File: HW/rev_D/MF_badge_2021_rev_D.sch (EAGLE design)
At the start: 80 parts, among them IC1 MCP73831, J1 HRO_31_M_12_USB_C, Q1 SI1308EDL-T1-GE3, Q2 DMG3415U-7, Q3 DMG3415U-7, Q4 DMG3415U-7, U1 ESP32-S2-WROOM, U2 AP2112K-3.3, X1 CAPTOUCH_10MM, X2 CAPTOUCH_10MM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

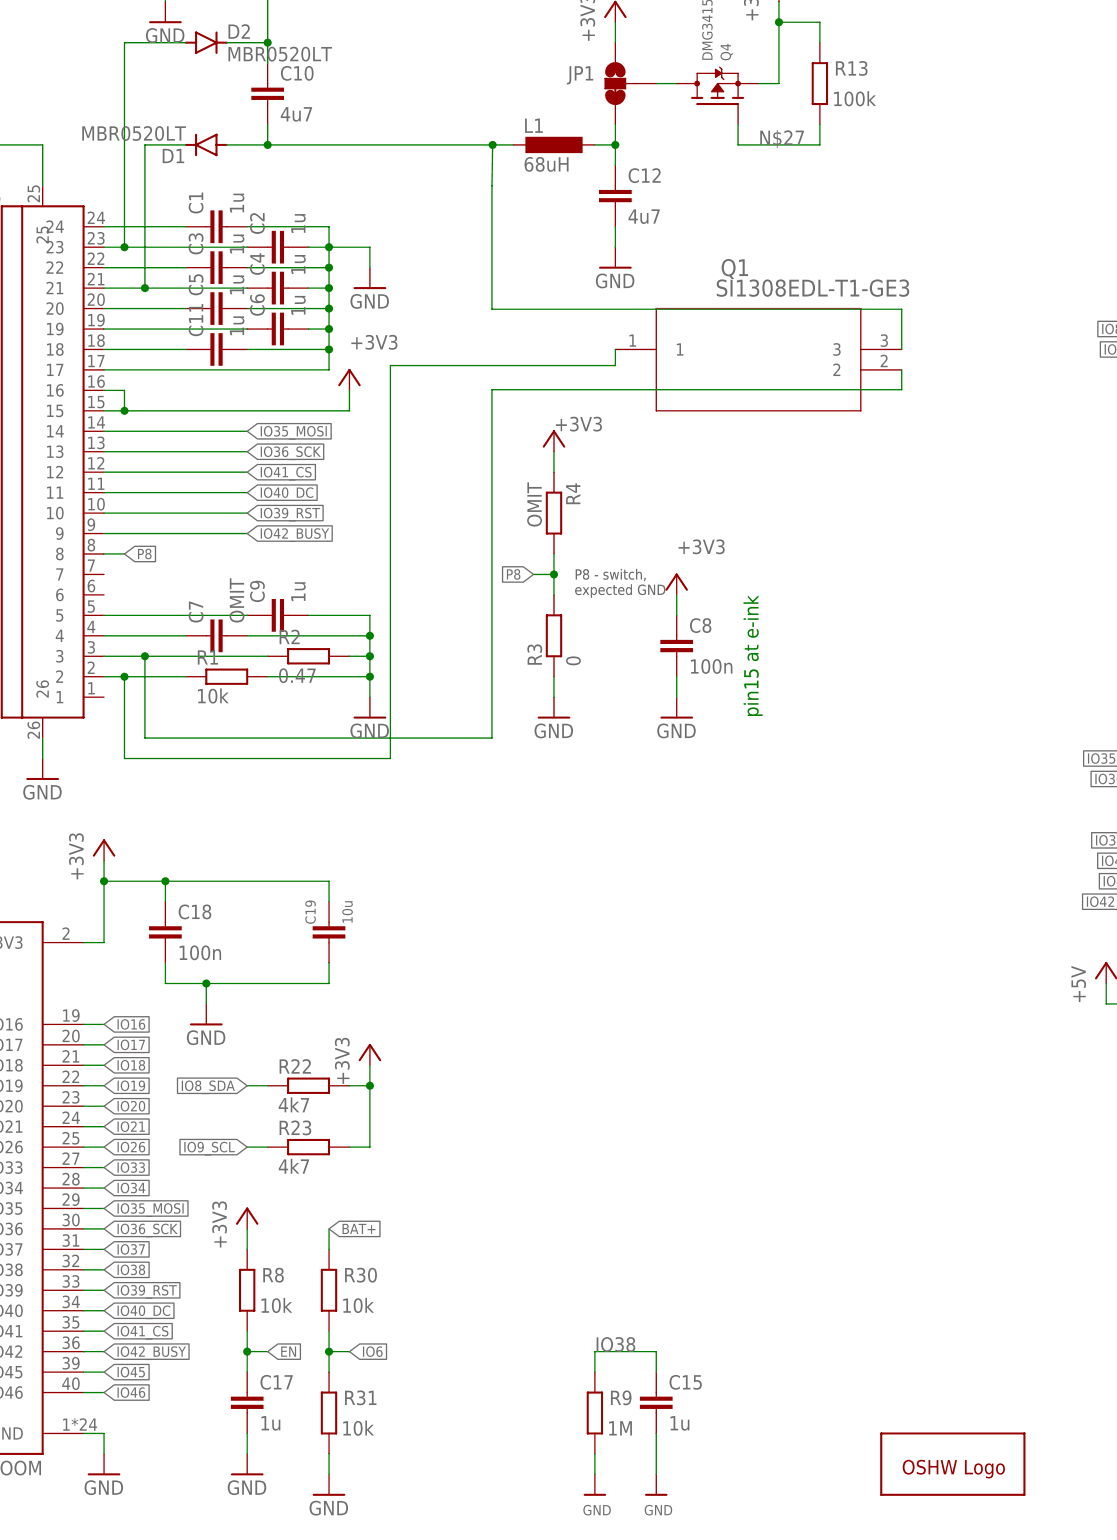
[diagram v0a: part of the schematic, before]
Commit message: Update
- removed CR2032 battery holder
- changed battery measuring circuit to save power
- add N-MOSFET to control 3V3 to e-ink displey
- changed QR to match new project address
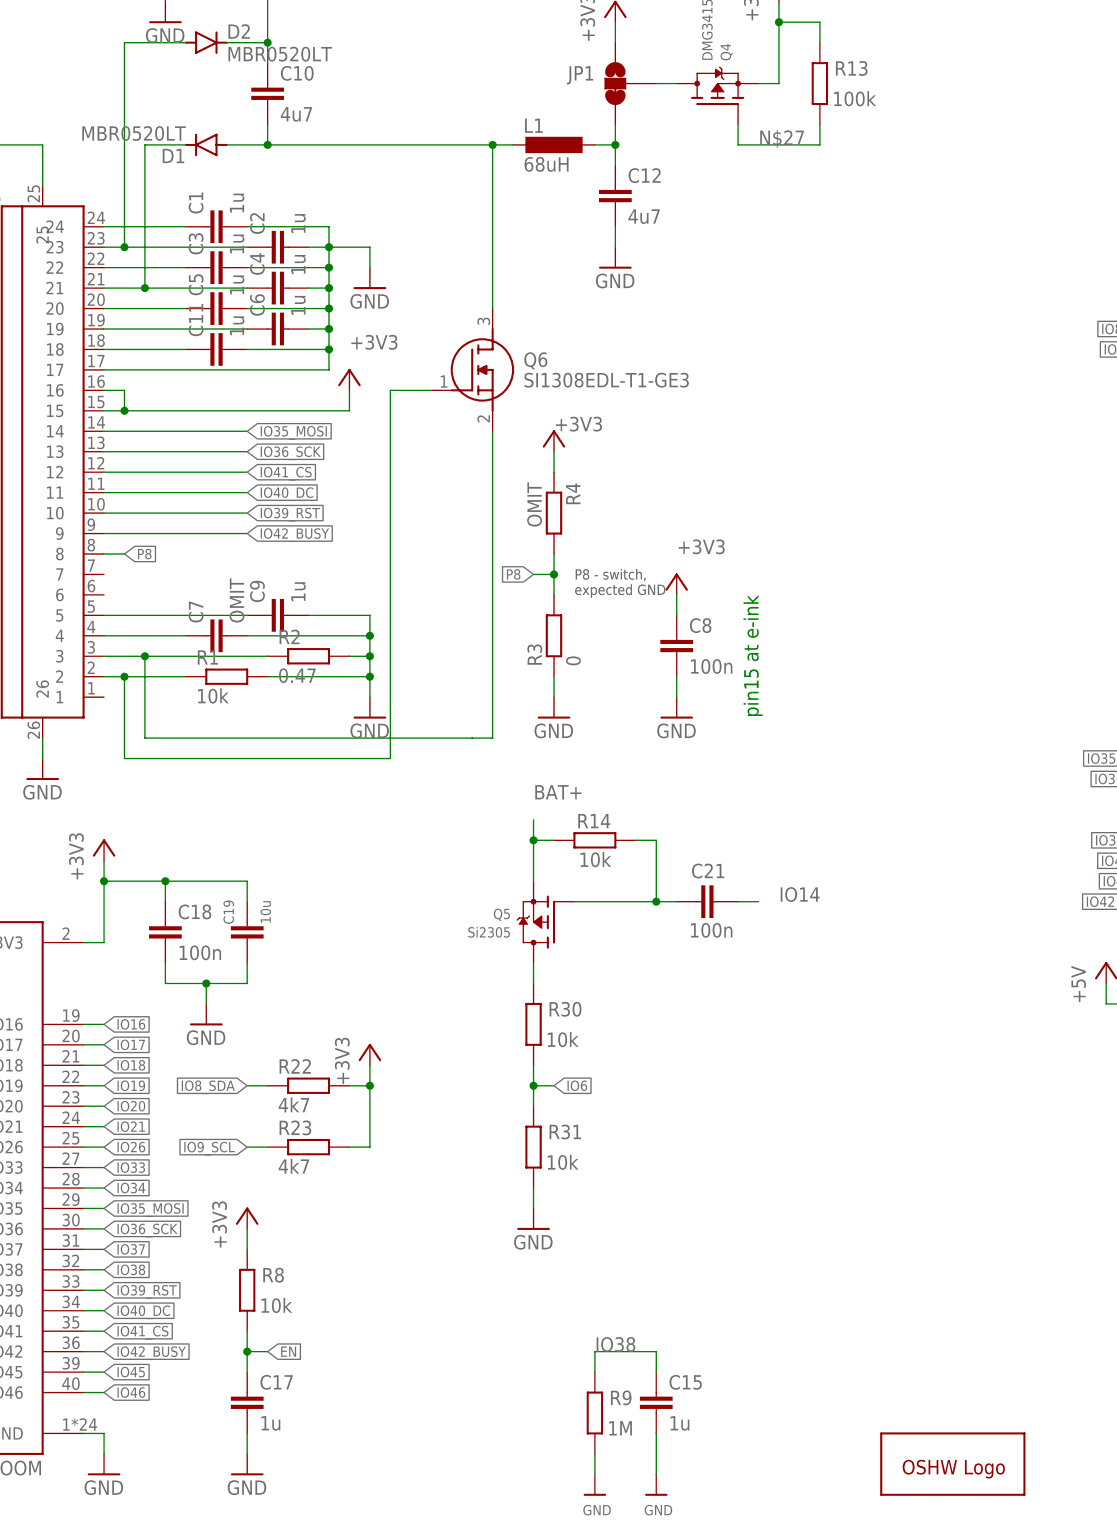
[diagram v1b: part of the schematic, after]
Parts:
- removed Q1: SI1308EDL-T1-GE3, SI1308EDL-T1-GE3:SI1308EDL-T1-GE3
- added C21: 100n, rcl:C-EUC0805
- added Q5: Si2305, microbuilder:MOSFET-P
- added Q6: SI1308EDL-T1-GE3, SamacSys_Parts:SI1308EDL-T1-GE3
- added R14: 10k, rcl:R-EU_R0805
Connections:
- new net N$79: Q5.D, R30.2
- new net N$80: C21.1, Q5.G, R14.1
- net BAT+: now also Q5.S, R14.2; no longer R30.2
- net IO14: now also C21.2
- net N$10: now also Q6.S; no longer Q1.2
- net N$13: now also Q6.G; no longer Q1.1
- net N$19: now also Q6.D; no longer Q1.3
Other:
- moved on the sheet: C19, R30, R31

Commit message: Update
- schematic cleanup
- power supply layout optimization
- changed some R and C values
- add hole for battery holder
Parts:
- C10, C12: value 4u7 -> 4u7F
- C13, C14, C16, C19, C20: value 10u -> 10uF
- C15, C17, C22, C9: value 1u -> 1uF
- C18: value 100n -> 10uF
- C21, C8: value 100n -> 100nF
- R1, R10, R11, R12, R14, R30, R31, R7, R8: value 10k -> 10K
- R13, R5: value 100k -> 10K
- R15, R16: value 5k1 -> 5K1
- R17, R18: value 22 -> 22R
- R2: value 0.47 -> 0.47R
- R22, R23: value 4k7 -> 4K7
- R6: value 1k -> 1K
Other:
- moved on the sheet: BOOT, C1, C10, C11, C12, C13, C14, C15, C16, C18, C19, C2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

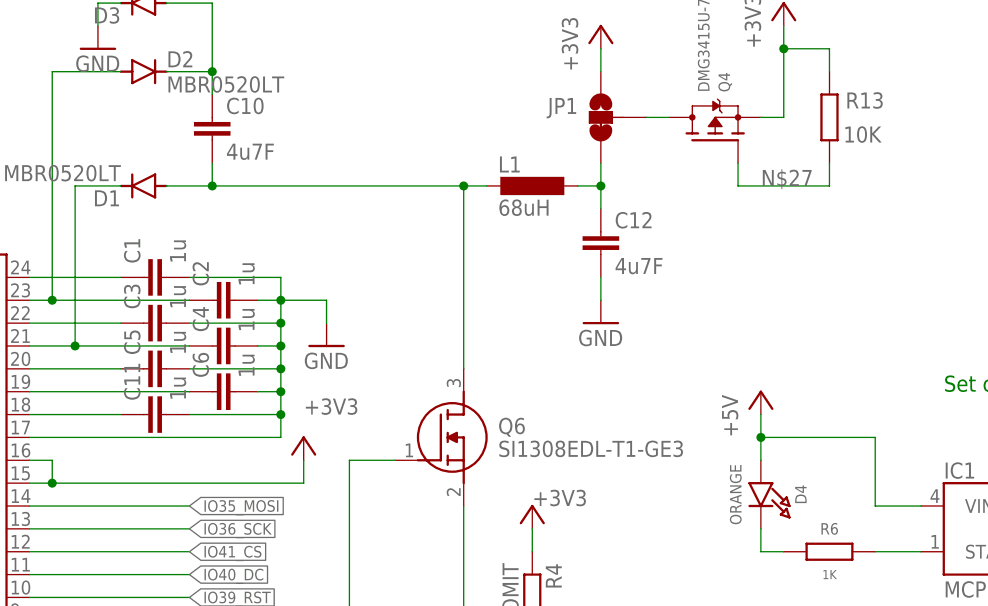
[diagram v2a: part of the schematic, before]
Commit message: Update MF_badge_2021_rev_D.sch
- forget to add it in previous commit
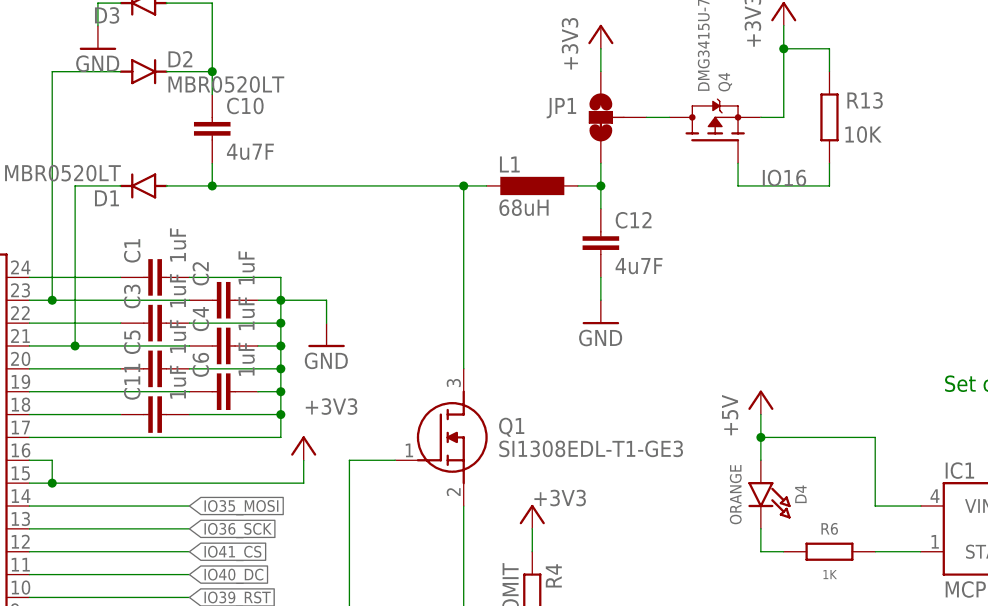
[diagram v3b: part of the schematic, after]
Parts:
- C1, C11, C2, C3, C4, C5, C6: value 1u -> 1uF
- renumbered Q6 to Q1
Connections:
- removed net N$27: Q4.G, R13.1
- net IO16: now also Q4.G, R13.1
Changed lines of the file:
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@@
 <part name="R1" library="rcl" library_urn="urn:adsk.eagle:library:334" deviceset="R-EU_" device="R0805" package3d_urn="urn:adsk.eagle:package:23553/2" value="10K"/>
 <part name="R2" library="rcl" library_urn="urn:adsk.eagle:library:334" deviceset="R-EU_" device="R0805" package3d_urn="urn:adsk.eagle:package:23553/2" value="0.47R"/>
-<part name="C1" library="rcl" library_urn="urn:adsk.eagle:library:334" deviceset="C-EU" device="C0805" package3d_urn="urn:adsk.eagle:package:23617/2" value="1u"/>
-<part name="C2" library="rcl" library_urn="urn:adsk.eagle:library:334" deviceset="C-EU" device="C0805" package3d_urn="urn:adsk.eagle:package:23617/2" value="1u"/>
-<part name="C3" library="rcl" library_urn="urn:adsk.eagle:library:334" deviceset="C-EU" device="C0805" package3d_urn="urn:adsk.eagle:package:23617/2" value="1u"/>
-<part name="C4" library="rcl" library_urn="urn:adsk.eagle:library:334" deviceset="C-EU" device="C0805" package3d_urn="urn:adsk.eagle:package:23617/2" value="1u"/>
-<part name="C5" library="rcl" library_urn="urn:adsk.eagle:library:334" deviceset="C-EU" device="C0805" package3d_urn="urn:adsk.eagle:package:23617/2" value="1u"/>
-<part name="C6" library="rcl" library_urn="urn:adsk.eagle:library:334" deviceset="C-EU" device="C0805" package3d_urn="urn:adsk.eagle:package:23617/2" value="1u"/>
+<part name="C1" library="rcl" library_urn="urn:adsk.eagle:library:334" deviceset="C-EU" device="C0805" package3d_urn="urn:adsk.eagle:package:23617/2" value="1uF"/>
+<part name="C2" library="rcl" library_urn="urn:adsk.eagle:library:334" deviceset="C-EU" device="C0805" package3d_urn="urn:adsk.eagle:package:23617/2" value="1uF"/>
+<part name="C3" library="rcl" library_urn="urn:adsk.eagle:library:334" deviceset="C-EU" device="C0805" package3d_urn="urn:adsk.eagle:package:23617/2" value="1uF"/>
+<part name="C4" library="rcl" library_urn="urn:adsk.eagle:library:334" deviceset="C-EU" device="C0805" package3d_urn="urn:adsk.eagle:package:23617/2" value="1uF"/>
+<part name="C5" library="rcl" library_urn="urn:adsk.eagle:library:334" deviceset="C-EU" device="C0805" package3d_urn="urn:adsk.eagle:package:23617/2" value="1uF"/>
+<part name="C6" library="rcl" library_urn="urn:adsk.eagle:library:334" deviceset="C-EU" device="C0805" package3d_urn="urn:adsk.eagle:package:23617/2" value="1uF"/>
 <part name="C7" library="rcl" library_urn="urn:adsk.eagle:library:334" deviceset="C-EU" device="C0805" package3d_urn="urn:adsk.eagle:package:23617/2" value="OMIT"/>
 <part name="C8" library="rcl" library_urn="urn:adsk.eagle:library:334" deviceset="C-EU" device="C0805" package3d_urn="urn:adsk.eagle:package:23617/2" value="100nF"/>
 <part name="C9" library="rcl" library_urn="urn:adsk.eagle:library:334" deviceset="C-EU" device="C0805" package3d_urn="urn:adsk.eagle:package:23617/2" value="1uF"/>
 <part name="C10" library="rcl" library_urn="urn:adsk.eagle:library:334" deviceset="C-EU" device="C0805" package3d_urn="urn:adsk.eagle:package:23617/2" value="4u7F"/>
-<part name="C11" library="rcl" library_urn="urn:adsk.eagle:library:334" deviceset="C-EU" device="C0805" package3d_urn="urn:adsk.eagle:package:23617/2" value="1u"/>
+<part name="C11" library="rcl" library_urn="urn:adsk.eagle:library:334" deviceset="C-EU" device="C0805" package3d_urn="urn:adsk.eagle:package:23617/2" value="1uF"/>
 <part name="C12" library="rcl" library_urn="urn:adsk.eagle:library:334" deviceset="C-EU" device="C0805" package3d_urn="urn:adsk.eagle:package:23617/2" value="4u7F"/>
 <part name="L1" library="rcl" library_urn="urn:adsk.eagle:library:334" deviceset="L-EU" device="L4532P" package3d_urn="urn:adsk.eagle:package:23484/1" value="68uH"/>
@@
 <part name="R14" library="rcl" library_urn="urn:adsk.eagle:library:334" deviceset="R-EU_" device="R0805" package3d_urn="urn:adsk.eagle:package:23553/2" value="10K"/>
 <part name="C21" library="rcl" library_urn="urn:adsk.eagle:library:334" deviceset="C-EU" device="C0805" package3d_urn="urn:adsk.eagle:package:23617/2" value="100nF"/>
-<part name="Q6" library="SamacSys_Parts" deviceset="SI1308EDL-T1-GE3" device=""/>
+<part name="Q1" library="SamacSys_Parts" deviceset="SI1308EDL-T1-GE3" device=""/>
 <part name="+3V13" library="supply1" library_urn="urn:adsk.eagle:library:371" deviceset="+3V3" device=""/>
 </parts>
@@
 <attribute name="VALUE" x="115.824" y="43.815" size="1.778" layer="96"/>
 </instance>
-<instance part="Q6" gate="G$1" x="63.5" y="149.86" smashed="yes">
+<instance part="Q1" gate="G$1" x="63.5" y="149.86" smashed="yes">
 <attribute name="NAME" x="74.93" y="153.67" size="1.778" layer="95" align="center-left"/>
 <attribute name="VALUE" x="74.93" y="151.13" size="1.778" layer="96" align="center-left"/>
@@
 <wire x1="27.94" y1="106.68" x2="27.94" y2="116.84" width="0.1524" layer="91"/>
 <junction x="27.94" y="116.84"/>
-<pinref part="Q6" gate="G$1" pin="S"/>
+<pinref part="Q1" gate="G$1" pin="S"/>
 <wire x1="71.12" y1="144.78" x2="71.12" y2="106.68" width="0.1524" layer="91"/>
 </segment>
@@
 <wire x1="25.4" y1="104.14" x2="25.4" y2="114.3" width="0.1524" layer="91"/>
 <junction x="25.4" y="114.3"/>
-<pinref part="Q6" gate="G$1" pin="G"/>
+<pinref part="Q1" gate="G$1" pin="G"/>
 <wire x1="63.5" y1="149.86" x2="58.42" y2="149.86" width="0.1524" layer="91"/>
 </segment>
@@
 <pinref part="GPIO2" gate="A" pin="19"/>
 </segment>
+<segment>
+<pinref part="Q4" gate="G$1" pin="G"/>
+<wire x1="101.6" y1="182.88" x2="101.6" y2="180.34" width="0.1524" layer="91"/>
+<wire x1="101.6" y1="180.34" x2="111.76" y2="180.34" width="0.1524" layer="91"/>
+<pinref part="R13" gate="G$1" pin="1"/>
+<wire x1="111.76" y1="182.88" x2="111.76" y2="180.34" width="0.1524" layer="91"/>
+<label x="104.14" y="180.34" size="1.778" layer="95"/>
+</segment>
 </net>
 <net name="IO17" class="0">
@@
 <junction x="43.18" y="180.34"/>
 <wire x1="71.12" y1="180.34" x2="73.66" y2="180.34" width="0.1524" layer="91"/>
-<pinref part="Q6" gate="G$1" pin="D"/>
+<pinref part="Q1" gate="G$1" pin="D"/>
 <wire x1="71.12" y1="160.02" x2="71.12" y2="180.34" width="0.1524" layer="91"/>
 <junction x="71.12" y="180.34"/>
@@
 </segment>
 </net>
-<net name="N$27" class="0">
-<segment>
-<pinref part="Q4" gate="G$1" pin="G"/>
-<wire x1="101.6" y1="182.88" x2="101.6" y2="180.34" width="0.1524" layer="91"/>
-<wire x1="101.6" y1="180.34" x2="111.76" y2="180.34" width="0.1524" layer="91"/>
-<pinref part="R13" gate="G$1" pin="1"/>
-<wire x1="111.76" y1="182.88" x2="111.76" y2="180.34" width="0.1524" layer="91"/>
-<label x="104.14" y="180.34" size="1.778" layer="95"/>
-</segment>
-</net>

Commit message: Verified design files for rev.D
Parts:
- removed JP1: JUMPER-SMT_3_1-NC_TRACE_NO-SILK, SparkFun-Jumpers:JUMPER-SMT_3_1-NC_TRACE_NO-SILK
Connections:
- removed net N$78: JP1.2, Q4.D
- net +3V3: no longer JP1.1
- net N$26: now also Q4.D; no longer JP1.3
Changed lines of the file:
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@@
 <part name="Q4" library="microbuilder" deviceset="MOSFET-P" device="" value="DMG3415U-7"/>
 <part name="R13" library="rcl" library_urn="urn:adsk.eagle:library:334" deviceset="R-EU_" device="R0805" package3d_urn="urn:adsk.eagle:package:23553/2" value="10K"/>
-<part name="JP1" library="SparkFun-Jumpers" deviceset="JUMPER-SMT_3_1-NC_TRACE" device="_NO-SILK"/>
-<part name="+3V12" library="supply1" library_urn="urn:adsk.eagle:library:371" deviceset="+3V3" device=""/>
 <part name="Q5" library="microbuilder" deviceset="MOSFET-P" device="" value="Si2305"/>
 <part name="R14" library="rcl" library_urn="urn:adsk.eagle:library:334" deviceset="R-EU_" device="R0805" package3d_urn="urn:adsk.eagle:package:23553/2" value="10K"/>
@@
 <attribute name="VALUE" x="113.284" y="185.166" size="1.778" layer="96"/>
 </instance>
-<instance part="JP1" gate="G$1" x="86.36" y="187.96" smashed="yes" rot="MR0">
-<attribute name="NAME" x="83.82" y="188.341" size="1.778" layer="95" font="vector" rot="MR0"/>
-</instance>
-<instance part="+3V12" gate="G$1" x="86.36" y="198.12" smashed="yes">
-<attribute name="VALUE" x="83.82" y="193.04" size="1.778" layer="96" rot="R90"/>
-</instance>
 <instance part="Q5" gate="G$1" x="96.52" y="45.72" smashed="yes" rot="MR0">
 <attribute name="VALUE" x="93.726" y="43.815" size="1.27" layer="96" rot="MR0"/>
@@
 <wire x1="111.76" y1="195.58" x2="106.68" y2="195.58" width="0.1524" layer="91"/>
 <junction x="106.68" y="195.58"/>
-</segment>
-<segment>
-<pinref part="+3V12" gate="G$1" pin="+3V3"/>
-<pinref part="JP1" gate="G$1" pin="1"/>
-<wire x1="86.36" y1="195.58" x2="86.36" y2="193.04" width="0.1524" layer="91"/>
 </segment>
 </net>
@@
 <wire x1="83.82" y1="180.34" x2="86.36" y2="180.34" width="0.1524" layer="91"/>
 <wire x1="86.36" y1="180.34" x2="86.36" y2="177.8" width="0.1524" layer="91"/>
-<pinref part="JP1" gate="G$1" pin="3"/>
-<wire x1="86.36" y1="182.88" x2="86.36" y2="180.34" width="0.1524" layer="91"/>
 <junction x="86.36" y="180.34"/>
-</segment>
-</net>
-<net name="N$78" class="0">
-<segment>
-<pinref part="JP1" gate="G$1" pin="2"/>
 <pinref part="Q4" gate="G$1" pin="D"/>
-<wire x1="91.44" y1="187.96" x2="93.98" y2="187.96" width="0.1524" layer="91"/>
-</segment>
-</net>
+<wire x1="93.98" y1="187.96" x2="86.36" y2="187.96" width="0.1524" layer="91"/>
+<wire x1="86.36" y1="187.96" x2="86.36" y2="180.34" width="0.1524" layer="91"/>
+</segment>
+</net>
